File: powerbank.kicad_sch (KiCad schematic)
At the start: 17 parts, among them U12 AT24CS08-STUM, U6 TPS25751DREFR_C30169739

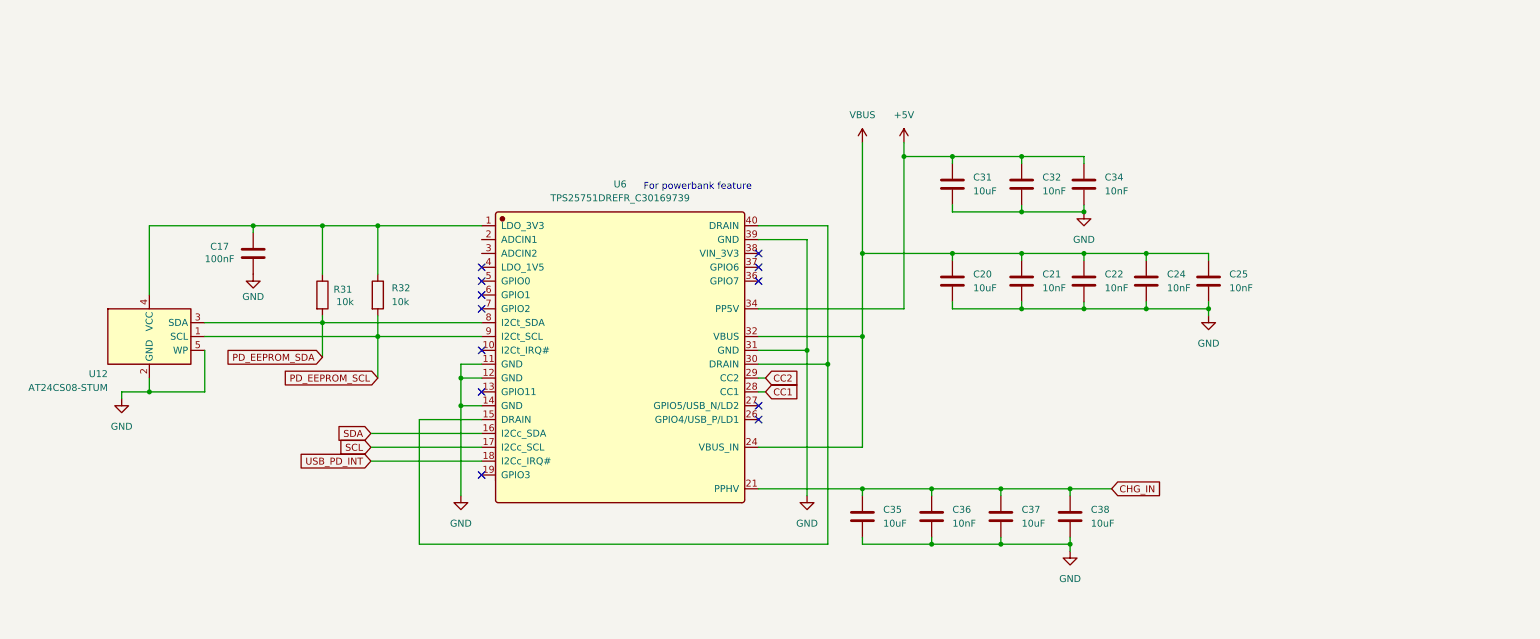
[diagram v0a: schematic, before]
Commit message: Refine board
* Add UART connector for chaining and controll
* shrink the board
workspace 1 output DP-6
* allow for pd controller eeprom programming
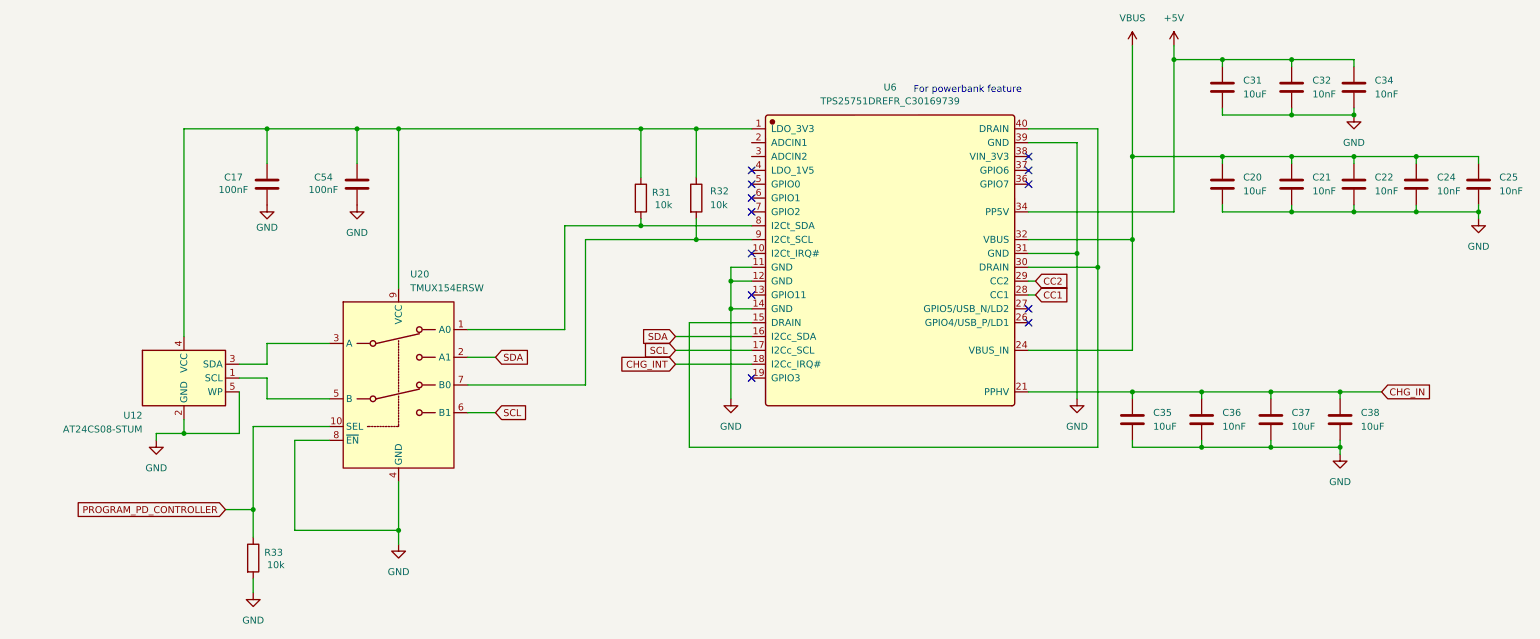
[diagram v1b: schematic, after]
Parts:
- added C54: 100nF, Capacitor_SMD:C_0402_1005Metric, symbol Device:C
- added R33: 10k, Resistor_SMD:R_0402_1005Metric, symbol Device:R
- added U20: TMUX154ERSW, Package_DFN_QFN:UQFN-10_1.4x1.8mm_P0.4mm, symbol Analog_Switch:TMUX154ERSW
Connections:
- net GND: now also C54.2, R33.2, U20.4 (GND), U20.8 (~{EN})
- net SCL: now also U20.6 (B1)
- net SDA: now also U20.2 (A1)
- net at C17.1, R31.1, R32.1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: now also C54.1, U20.9 (VCC)
- net PD_EEPROM_SCL: no longer names the net of R32.2, U6.9 (I2Ct_SCL)
- net PD_EEPROM_SCL: now also U20.7 (B0); no longer U12.1 (SCL)
- net PD_EEPROM_SDA: no longer names the net of R31.2, U6.8 (I2Ct_SDA)
- net PD_EEPROM_SDA: now also U20.1 (A0); no longer U12.3 (SDA)
- net USB_PD_INT renamed CHG_INT
- new net: U12.3 (SDA), U20.3 (A)
- new net: U12.1 (SCL), U20.5 (B)
- new net PROGRAM_PD_CONTROLLER: R33.1, U20.10 (SEL)
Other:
- moved on the sheet: C17, C20, C21, C22, C24, C25, C31, C32, C34, C35, C36, C37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
